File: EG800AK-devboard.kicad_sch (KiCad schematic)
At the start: 46 parts, among them J1 U.FL-R-SMT_10_, J2 MICROQTJ, J4 Conn_01x11_Pin, Q1 DTC143ZUAT106, Q2 DTC143ZUAT106, Q4 DTC143ZUAT106, Q5 DTC143ZUAT106, SW1 TS-1088-AR02016, U1 EG800KEULC-I03-SNNSA, U2 GPS1003

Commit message: carga
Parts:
- C17, C7, C8: value 470uF -> 100uF

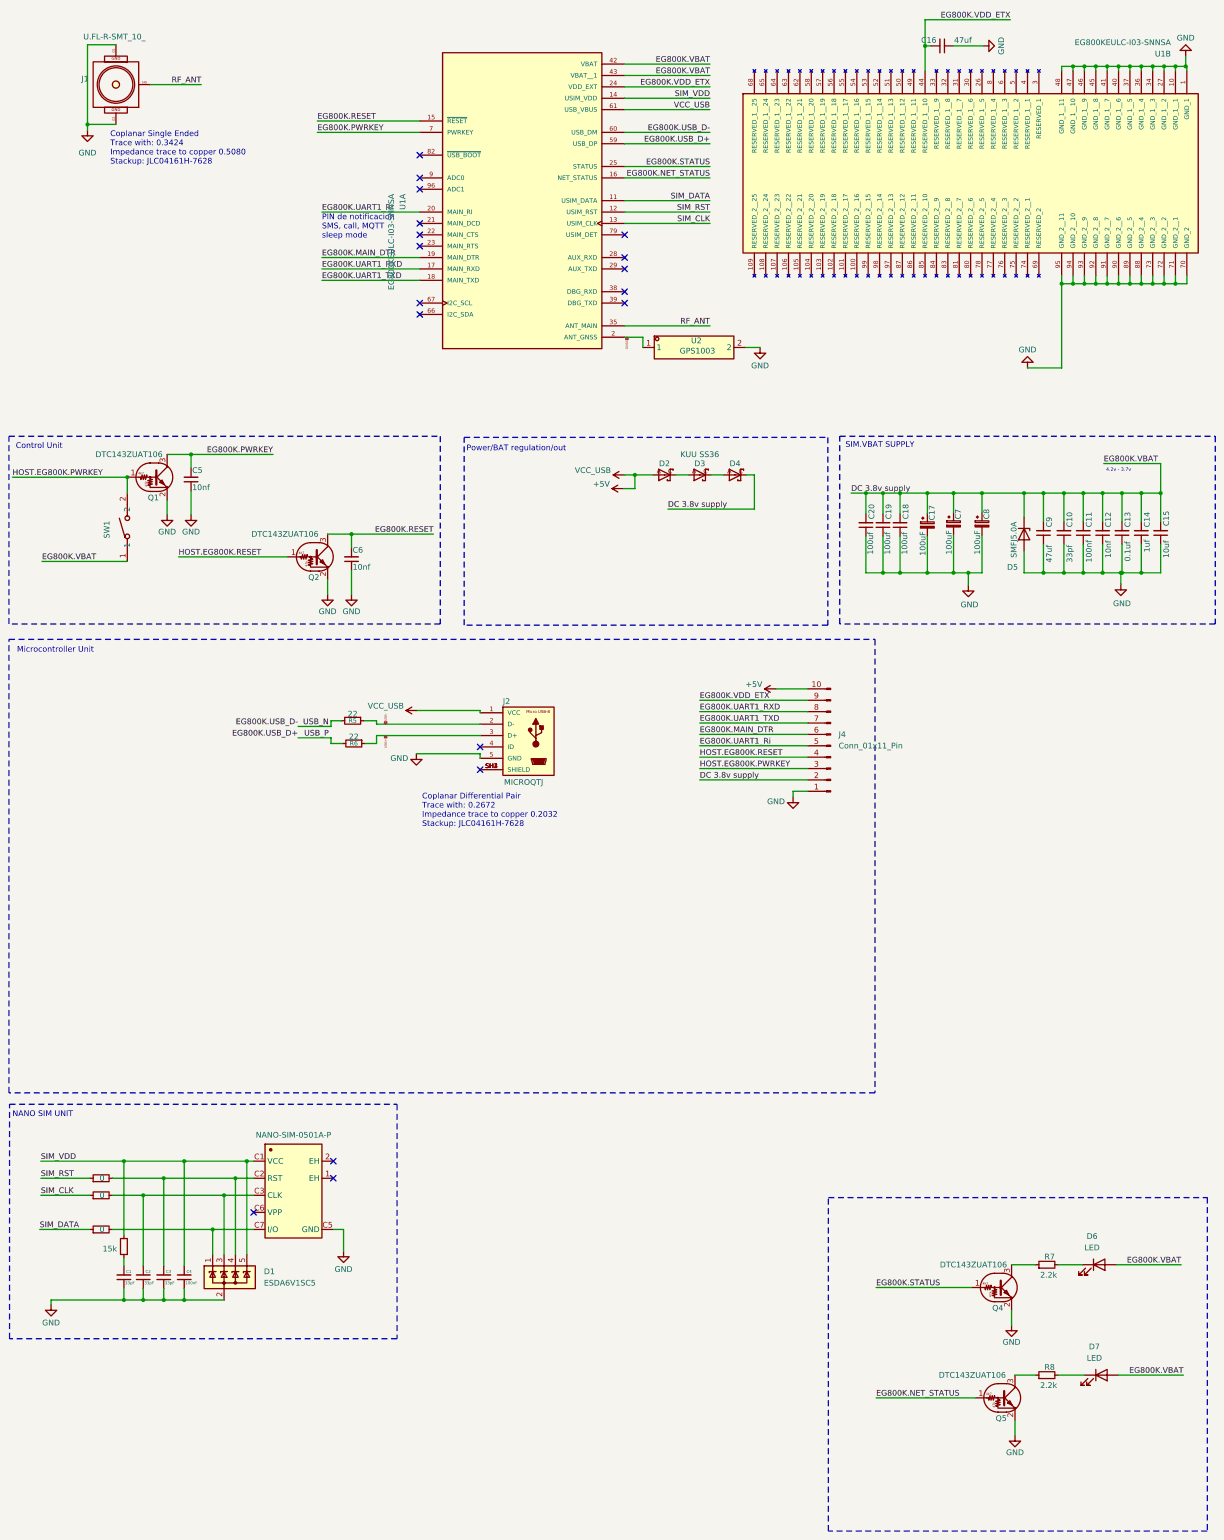
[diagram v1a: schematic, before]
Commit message: Eliminacion de GNSS, correcion final en nano_sim
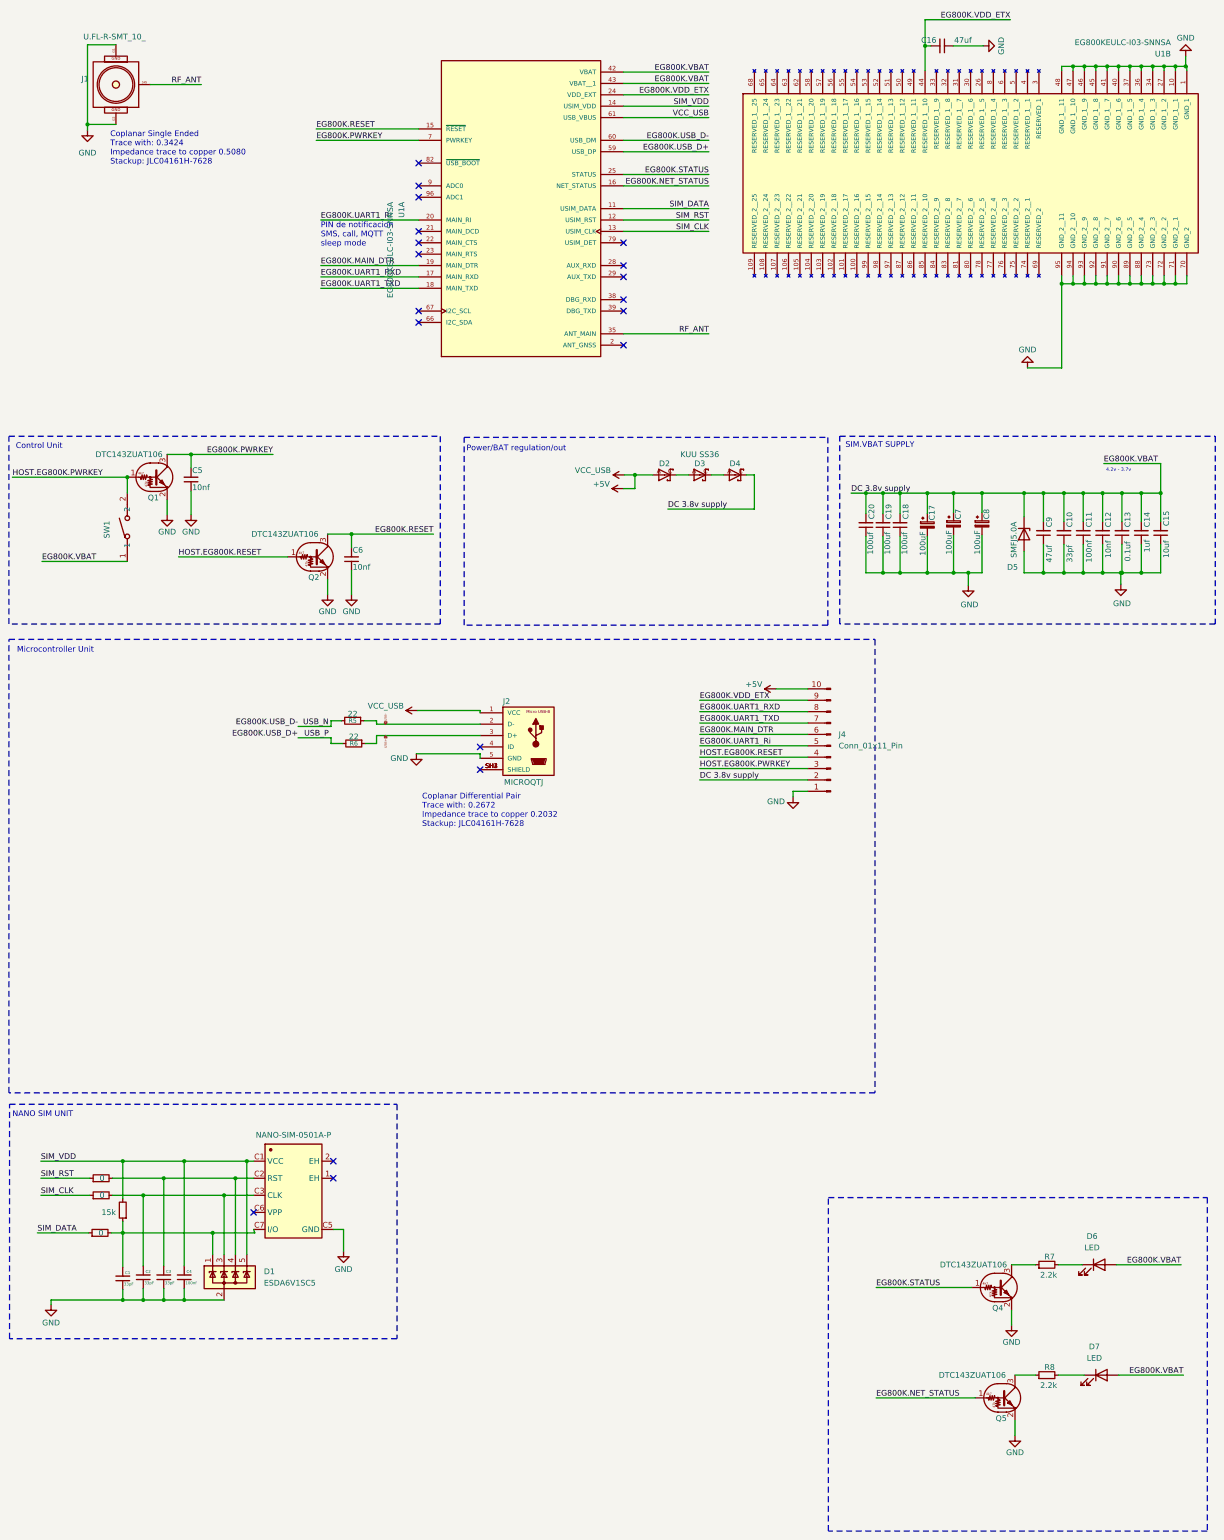
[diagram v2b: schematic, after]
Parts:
- removed U2: GPS1003, EasyEDA:ANT-SMD_L10.0-W3.0, symbol EasyEDA:GPS1003
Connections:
- net at D1.1 (K), NANO-SIM-0501A-P1.C7 (I/O), R3.2: now also C1.2, R4.1
- net GNSS: no longer names the net of U1.2 (ANT_GNSS)
- no-connect marks 18 -> 19
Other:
- moved on the sheet: U1A

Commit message: cambios finales
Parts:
- R7, R8: value 2.2k -> 3k
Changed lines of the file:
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@@
 			)
 		)
-		(property "Value" "2.2k"
+		(property "Value" "3k"
 			(at 247.904 322.326 90)
 			(show_name no)
@@
 			)
 		)
-		(property "Value" "2.2k"
+		(property "Value" "3k"
 			(at 247.904 297.688 90)
 			(show_name no)
